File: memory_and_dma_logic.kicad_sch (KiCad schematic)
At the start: 46 parts, among them U12 LS393, U13 LS157, U14 LS153, U15 4116, U16 4116, U22 LS393, U23 LS157, U24 LS153, U25 4116, U26 4116, U33 LS161, U34 LS153, U35 4116, U36 4116, U43 LS161, U44 LS153, U45 4116, U46 4116, U53 LS04, U6 LS741, U62 LS08

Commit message: Schematic corrections
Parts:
- C66, C94: footprint (none) -> K_1013_Jumper:C_Disc_D7.0mm_W2.5mm_P6.35mm
- R11: footprint Resistor_THT:R_Axial_DIN0207_L6.3mm_D2.5mm_P10.16mm_Horizontal -> K_1013_Jumper:R_Axial_DIN0309_L9.0mm_D3.2mm_P12.70mm_Horizontal
- U12, U22, U53, U62: footprint (none) -> K_1013_Jumper:DIP-14_W7.62mm_LongPads
- U13, U14, U15, U16, U23, U24, U25, U26, U33, U34, U35, U36, U43, U44, U45, U46: footprint (none) -> K_1013_Jumper:DIP-16_W7.62mm_LongPads
- U6: footprint Package_DIP:DIP-20_W7.62mm_LongPads -> K_1013_Jumper:DIP-20_W7.62mm_LongPads

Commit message: Update progress
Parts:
- C20, C21, C22, C23, C34, C35, C36, C37, C47, C48, C49, C50, C61, C62, C63, C64: renamed from C94; footprint K_1013_Jumper:C_Disc_D7.0mm_W2.5mm_P6.35mm -> K_1013:C_Disc_D7.0mm_W2.5mm_P6.35mm
- C24, C38, C51, C58, C65, C77: renamed from C66; footprint K_1013_Jumper:C_Disc_D7.0mm_W2.5mm_P6.35mm -> K_1013:C_Disc_D7.0mm_W2.5mm_P6.35mm
- R15, R20, R21: renamed from R11; footprint K_1013_Jumper:R_Axial_DIN0309_L9.0mm_D3.2mm_P12.70mm_Horizontal -> K_1013:R_Axial_DIN0309_L9.0mm_D3.2mm_P12.70mm_Horizontal
- U12, U22, U53, U62: footprint K_1013_Jumper:DIP-14_W7.62mm_LongPads -> K_1013:DIP-14_W7.62mm_LongPads
- U13, U14, U15, U16, U23, U24, U25, U26, U33, U34, U35, U36, U43, U44, U45, U46: footprint K_1013_Jumper:DIP-16_W7.62mm_LongPads -> K_1013:DIP-16_W7.62mm_LongPads
- U6: footprint K_1013_Jumper:DIP-20_W7.62mm_LongPads -> K_1013:DIP-20_W7.62mm_LongPads

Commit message: Routing of the bottom layer completed
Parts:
- U12: footprint K_1013:DIP-14_W7.62mm_LongPads -> K_1013:DIP-14_W7.62mm_LongPads_U12
- U13: footprint K_1013:DIP-16_W7.62mm_LongPads -> K_1013:DIP-16_W7.62mm_LongPads_U13
- U22: footprint K_1013:DIP-14_W7.62mm_LongPads -> K_1013:DIP-14_W7.62mm_LongPads_U22
- U23: footprint K_1013:DIP-16_W7.62mm_LongPads -> K_1013:DIP-16_W7.62mm_LongPads_U23
- U24: footprint K_1013:DIP-16_W7.62mm_LongPads -> K_1013:DIP-16_W7.62mm_LongPads_U24
- U33: footprint K_1013:DIP-16_W7.62mm_LongPads -> K_1013:DIP-16_W7.62mm_LongPads_U33
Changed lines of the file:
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@@
       (effects (font (size 1.27 1.27)))
     )
-    (property "Footprint" "K_1013:DIP-14_W7.62mm_LongPads" (at 90.805 200.66 0)
+    (property "Footprint" "K_1013:DIP-14_W7.62mm_LongPads_U22" (at 90.805 200.66 0)
       (effects (font (size 1.27 1.27)) hide)
     )
@@
       (effects (font (size 1.27 1.27)))
     )
-    (property "Footprint" "K_1013:DIP-16_W7.62mm_LongPads" (at 368.3 194.31 0)
+    (property "Footprint" "K_1013:DIP-16_W7.62mm_LongPads_U24" (at 368.3 194.31 0)
       (effects (font (size 1.27 1.27)) hide)
     )
@@
       (effects (font (size 1.27 1.27)))
     )
-    (property "Footprint" "K_1013:DIP-14_W7.62mm_LongPads" (at 90.805 254 0)
+    (property "Footprint" "K_1013:DIP-14_W7.62mm_LongPads_U12" (at 90.805 254 0)
       (effects (font (size 1.27 1.27)) hide)
     )
@@
       (effects (font (size 1.27 1.27)))
     )
-    (property "Footprint" "K_1013:DIP-16_W7.62mm_LongPads" (at 231.14 242.57 0)
+    (property "Footprint" "K_1013:DIP-16_W7.62mm_LongPads_U13" (at 231.14 242.57 0)
       (effects (font (size 1.27 1.27)) hide)
     )
@@
       (effects (font (size 1.27 1.27)))
     )
-    (property "Footprint" "K_1013:DIP-16_W7.62mm_LongPads" (at 231.14 209.55 0)
+    (property "Footprint" "K_1013:DIP-16_W7.62mm_LongPads_U23" (at 231.14 209.55 0)
       (effects (font (size 1.27 1.27)) hide)
     )
@@
       (effects (font (size 1.27 1.27)))
     )
-    (property "Footprint" "K_1013:DIP-16_W7.62mm_LongPads" (at 231.14 176.53 0)
+    (property "Footprint" "K_1013:DIP-16_W7.62mm_LongPads_U33" (at 231.14 176.53 0)
       (effects (font (size 1.27 1.27)) hide)
     )
@@
       (effects (font (size 1.27 1.27)))
     )
-    (property "Footprint" "K_1013:DIP-14_W7.62mm_LongPads" (at 90.805 236.22 0)
+    (property "Footprint" "K_1013:DIP-14_W7.62mm_LongPads_U12" (at 90.805 236.22 0)
       (effects (font (size 1.27 1.27)) hide)
     )
@@
       (effects (font (size 1.27 1.27)))
     )
-    (property "Footprint" "K_1013:DIP-14_W7.62mm_LongPads" (at 90.805 218.44 0)
-      (effects (font (size 1.27 1.27)) hide)
-    )
+    (property "Footprint" "K_1013:DIP-14_W7.62mm_LongPads_U22" (at 90.805 218.44 0)
+      (effects (font (size 1.27 1.27)) hide)
+    )

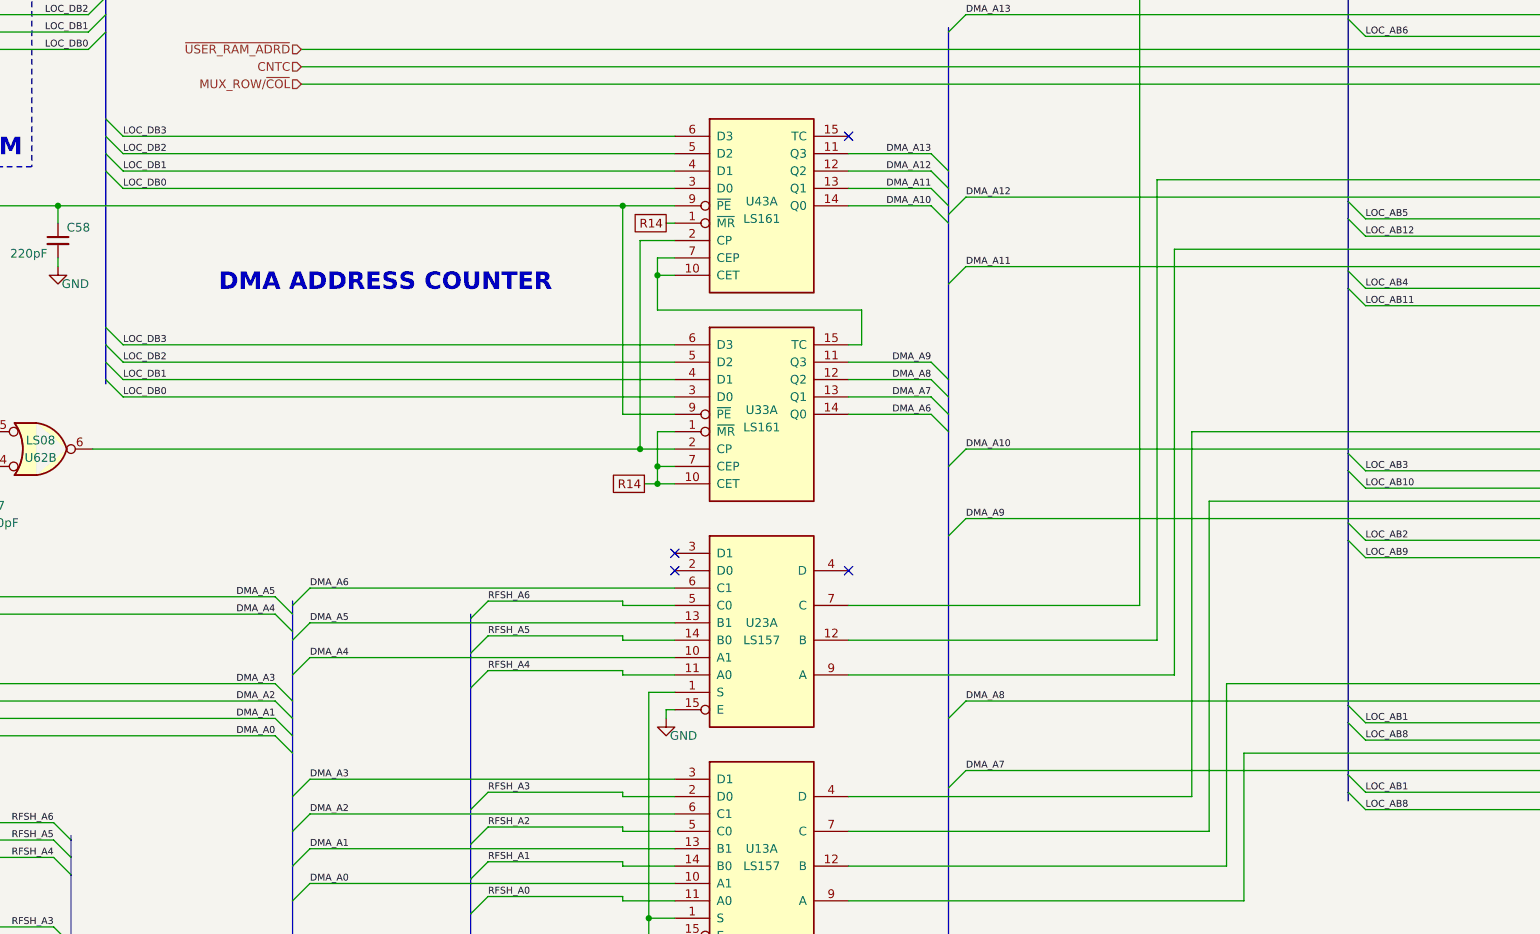
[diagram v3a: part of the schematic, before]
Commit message: Completed first version of board routing
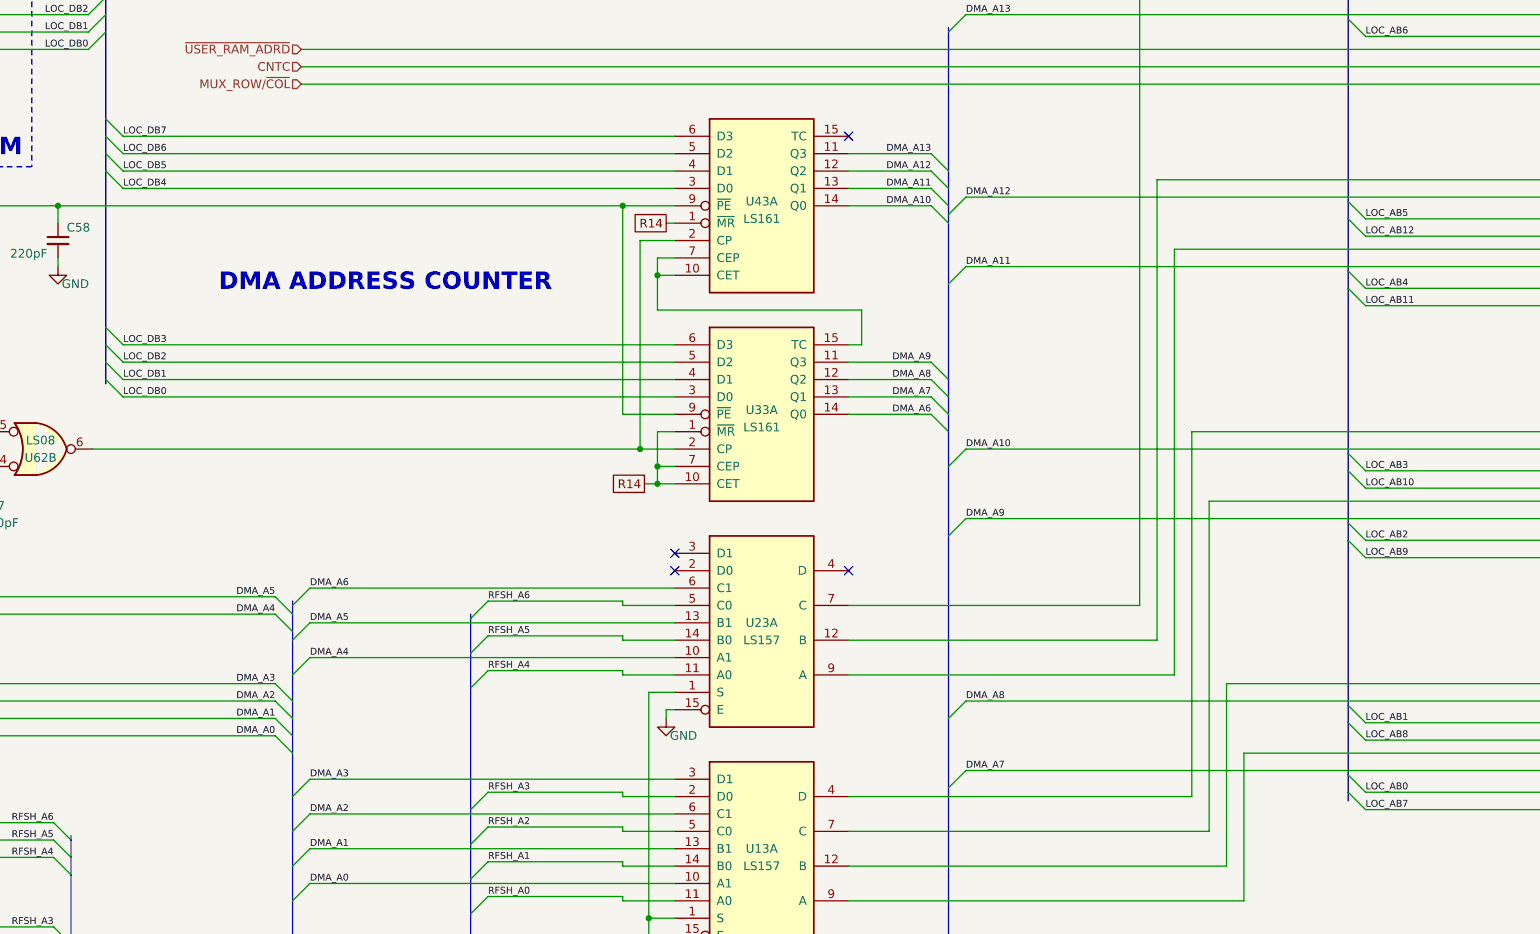
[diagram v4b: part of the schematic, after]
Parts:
- R15: footprint K_1013:R_Axial_DIN0309_L9.0mm_D3.2mm_P12.70mm_Horizontal -> K_1013:R_Axial_DIN0204_L3.6mm_D2.5mm_P12.70mm_Horizontal_470R
- R20: footprint K_1013:R_Axial_DIN0309_L9.0mm_D3.2mm_P12.70mm_Horizontal -> K_1013:R_Axial_DIN0204_L3.6mm_D2.5mm_P12.70mm_Horizontal_2K2
- R21: footprint K_1013:R_Axial_DIN0309_L9.0mm_D3.2mm_P12.70mm_Horizontal -> K_1013:R_Axial_DIN0204_L3.6mm_D2.5mm_P12.70mm_Horizontal_3K3
- U6: footprint K_1013:DIP-20_W7.62mm_LongPads -> K_1013:DIP-20_W7.62mm_LongPads_U6
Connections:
- net LOC_AB0: now also U14.5 (I1a)
- net LOC_AB1: no longer U14.5 (I1a)
- net LOC_AB7: now also U14.6 (I0a)
- net LOC_AB8: no longer U14.6 (I0a)
- net LOC_DB0: no longer U43.3 (D0)
- net LOC_DB1: no longer U43.4 (D1)
- net LOC_DB2: no longer U43.5 (D2)
- net LOC_DB3: no longer U43.6 (D3)
- net LOC_DB4: now also U43.3 (D0)
- net LOC_DB5: now also U43.4 (D1)
- net LOC_DB6: now also U43.5 (D2)
- net LOC_DB7: now also U43.6 (D3)
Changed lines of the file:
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@@
     (effects (font (size 2.54 2.54) (thickness 0.508) bold) (justify left bottom))
   )
-  (label "LOC_AB1" (at 319.405 229.235 0) (fields_autoplaced)
+  (label "LOC_AB0" (at 319.405 229.235 0) (fields_autoplaced)
     (effects (font (size 1 1)) (justify left bottom))
   )
@@
     (effects (font (size 1 1)) (justify right bottom))
   )
-  (label "LOC_DB1" (at 137.795 138.43 0) (fields_autoplaced)
+  (label "LOC_DB5" (at 137.795 138.43 0) (fields_autoplaced)
     (effects (font (size 1 1)) (justify left bottom))
   )
@@
     (effects (font (size 1 1)) (justify left bottom))
   )
-  (label "LOC_AB8" (at 319.405 231.775 0) (fields_autoplaced)
+  (label "LOC_AB7" (at 319.405 231.775 0) (fields_autoplaced)
     (effects (font (size 1 1)) (justify left bottom))
   )
@@
     (effects (font (size 1 1)) (justify right bottom))
   )
-  (label "LOC_DB2" (at 137.795 135.89 0) (fields_autoplaced)
+  (label "LOC_DB6" (at 137.795 135.89 0) (fields_autoplaced)
     (effects (font (size 1 1)) (justify left bottom))
   )
@@
     (effects (font (size 1 1)) (justify right bottom))
   )
-  (label "LOC_DB3" (at 137.795 133.35 0) (fields_autoplaced)
+  (label "LOC_DB7" (at 137.795 133.35 0) (fields_autoplaced)
     (effects (font (size 1 1)) (justify left bottom))
   )
@@
     (effects (font (size 1 1)) (justify left bottom))
   )
-  (label "LOC_DB0" (at 137.795 140.97 0) (fields_autoplaced)
+  (label "LOC_DB4" (at 137.795 140.97 0) (fields_autoplaced)
     (effects (font (size 1 1)) (justify left bottom))
   )
@@
       (effects (font (size 1.27 1.27)))
     )
-    (property "Footprint" "K_1013:R_Axial_DIN0309_L9.0mm_D3.2mm_P12.70mm_Horizontal" (at 114.3 149.225 0)
+    (property "Footprint" "K_1013:R_Axial_DIN0204_L3.6mm_D2.5mm_P12.70mm_Horizontal_470R" (at 114.3 149.225 0)
       (effects (font (size 1.27 1.27)) hide)
     )
@@
       (effects (font (size 1.27 1.27)))
     )
-    (property "Footprint" "K_1013:DIP-20_W7.62mm_LongPads" (at 90.805 115.57 0)
+    (property "Footprint" "K_1013:DIP-20_W7.62mm_LongPads_U6" (at 90.805 115.57 0)
       (effects (font (size 1.27 1.27)) hide)
     )
@@
       (effects (font (size 1.27 1.27)))
     )
-    (property "Footprint" "K_1013:R_Axial_DIN0309_L9.0mm_D3.2mm_P12.70mm_Horizontal" (at 107.95 168.91 0)
+    (property "Footprint" "K_1013:R_Axial_DIN0204_L3.6mm_D2.5mm_P12.70mm_Horizontal_2K2" (at 107.95 168.91 0)
       (effects (font (size 1.27 1.27)) hide)
     )
@@
       (effects (font (size 1.27 1.27)))
     )
-    (property "Footprint" "K_1013:R_Axial_DIN0309_L9.0mm_D3.2mm_P12.70mm_Horizontal" (at 107.95 189.23 0)
+    (property "Footprint" "K_1013:R_Axial_DIN0204_L3.6mm_D2.5mm_P12.70mm_Horizontal_3K3" (at 107.95 189.23 0)
       (effects (font (size 1.27 1.27)) hide)
     )
